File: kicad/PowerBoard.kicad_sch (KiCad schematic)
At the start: 177 parts, among them IC1 LT1910ES8#PBF, IC2 LT1910ES8#PBF, IC3 LT1910ES8#PBF, IC4 LT1910ES8#PBF, IC5 LT1910ES8#PBF, IC7 MAX17541GATB+T, J1 XT90, J10 XT90, J11 XT90, J12 XT90, J13 XT90, J14 DEAN_T, J15 DEAN_T, J16 DEAN_T, J17 DEAN_T, J18 DEAN_T, J19 DEAN_T, J2 DEAN_T, J20 XT60, J21 XT60, J22 XT60, J23 XT60, J24 XT60, J25 XT60, J26 XT60, J27 XT60, J28 XT60, J29 XT60, J3 XT60, J30 XT60, J31 XT60, J32 XT30, J33 XT30, J34 XT30, J35 XT30, J36 XT30, J37 XT30, J38 XT30, J39 XT30, J4 XT30, J40 XT30, J41 XT60, J5 Conn_01x02, J6 XT90, J7 XT90, J8 XT90, J9 XT90, Q1 IRFS7530TRL7PP, Q2 IRFS7437TRLPBF, Q3 IRFS7437TRLPBF, Q4 IRFS7437TRLPBF, Q5 IRFS7437TRLPBF, U1 Pico, U2 INA238, U3 INA238, U4 INA238, U5 INA238, U6 INA238

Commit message: finish v2.4.0
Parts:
- added J42, J43: DEAN_T, SamacSys_Parts:DEANS-T, symbol Connector_Generic:Conn_01x02
- added J44, J45, J46: XT60, Connector_AMASS:AMASS_XT60-F_1x02_P7.20mm_Vertical, symbol Connector_Generic:Conn_01x02
- added J47, J48: XT30, Connector_AMASS:AMASS_XT30U-F_1x02_P5.0mm_Vertical, symbol Connector_Generic:Conn_01x02
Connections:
- net 12V_2: now also J46.2 (Pin_2)
- net 15V_2: now also J44.2 (Pin_2), J45.2 (Pin_2)
- net 24V_2: now also J42.2 (Pin_2), J43.2 (Pin_2)
- net 5V_2: now also J47.2 (Pin_2), J48.2 (Pin_2)
- net GND: now also J42.1 (Pin_1), J43.1 (Pin_1), J44.1 (Pin_1), J45.1 (Pin_1), J46.1 (Pin_1), J47.1 (Pin_1), J48.1 (Pin_1)
- net IC5-SENSE: now reaches C16.2, D24.2 (A), IC5.6 (SENSE), R46.1
- net IC3-SENSE: now reaches C14.1, D22.2 (A), IC3.6 (SENSE), R44.2
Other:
- moved on the sheet: D10, D9

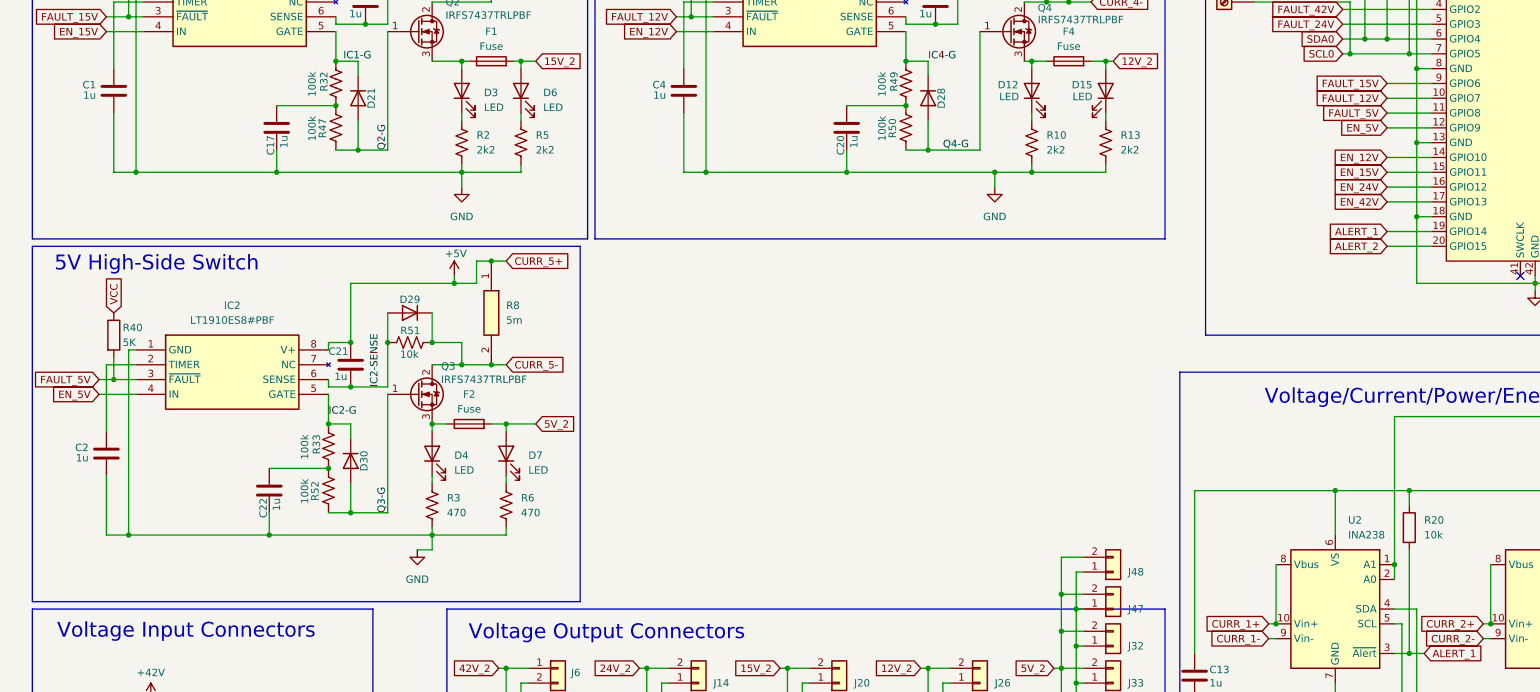
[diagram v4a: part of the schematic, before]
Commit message: rework the 5V switching
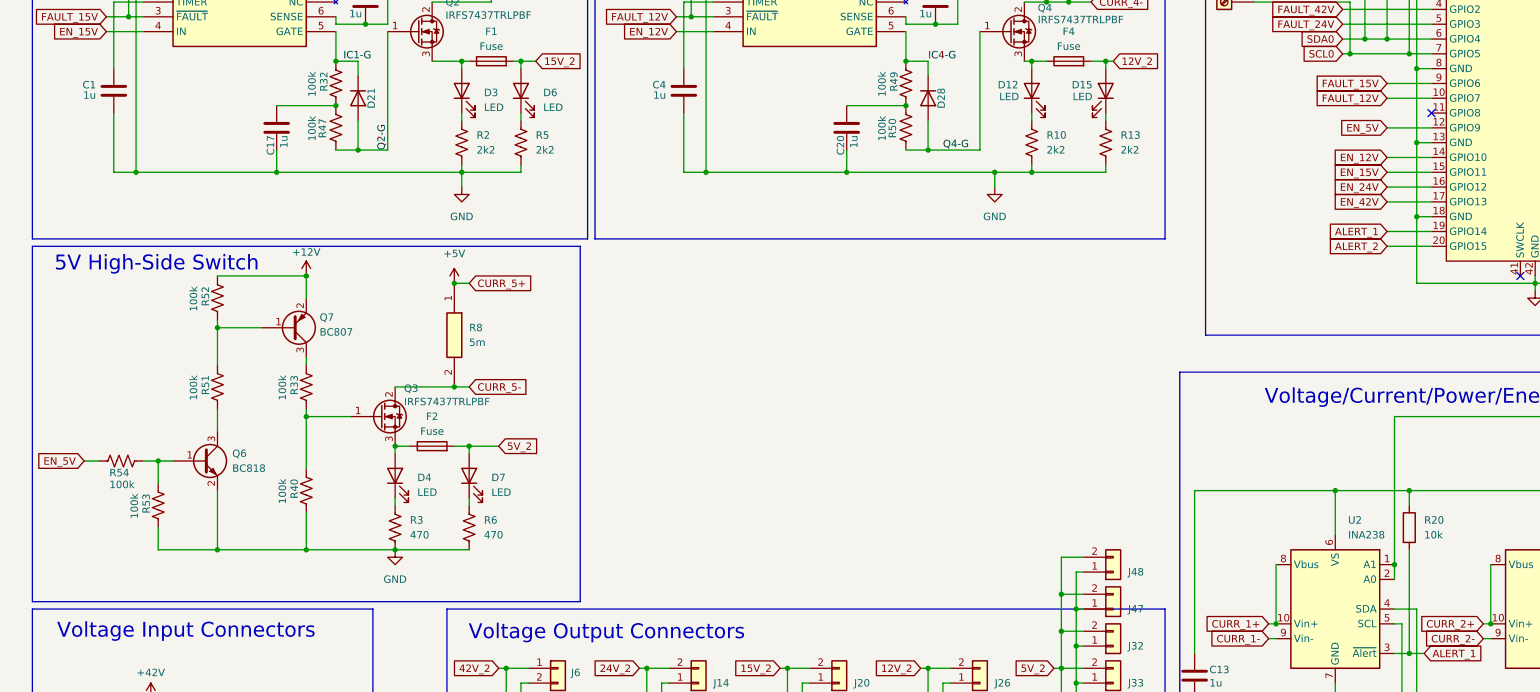
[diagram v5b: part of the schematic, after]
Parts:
- removed C2, C21, C22: 1u, Capacitor_SMD:C_0603_1608Metric, symbol Device:C
- removed D29, D30: 1N4148WT, Diode_SMD:D_SOD-523, symbol Diode:1N4148WT
- removed IC2: LT1910ES8#PBF, SOIC127P599X175-8N, symbol SamacSys_Parts:LT1910ES8#PBF
- removed R40: 5K, Resistor_SMD:R_1206_3216Metric, symbol Device:R
- added Q6: BC818, Package_TO_SOT_SMD:SOT-23, symbol Transistor_BJT:BC818
- added Q7: BC807, Package_TO_SOT_SMD:SOT-23, symbol Transistor_BJT:BC807
- added R40, R53, R54: 100k, Resistor_SMD:R_0603_1608Metric, symbol Device:R_US
- R51: value 10k -> 100k
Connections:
- net +12V: now also R52.2, Q7.2 (E)
- net CURR_5-: no longer R51.2
- net EN_5V: now also R54.2
- net GND: now also Q6.2 (E), R40.1, R53.1
- net at R52.1: now also R51.2, Q7.1 (B); no longer R33.1
- net FAULT_5V: no longer names the net of U1.11 (GPIO8)
- net IC2-G: no longer names the net of R33.2
- net IC2-G: now also Q7.3 (C)
- net IC2-SENSE: no longer names the net of R51.1
- net IC2-SENSE: now also Q6.3 (C)
- net Q3-G: no longer names the net of Q3.1 (G)
- net Q3-G: now also R33.1, R40.2; no longer R52.2
- new net: Q6.1 (B), R53.2, R54.1
- no-connect marks 10 -> 11
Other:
- moved on the sheet: D4, D7, F2, Q3, R3, R6, R8

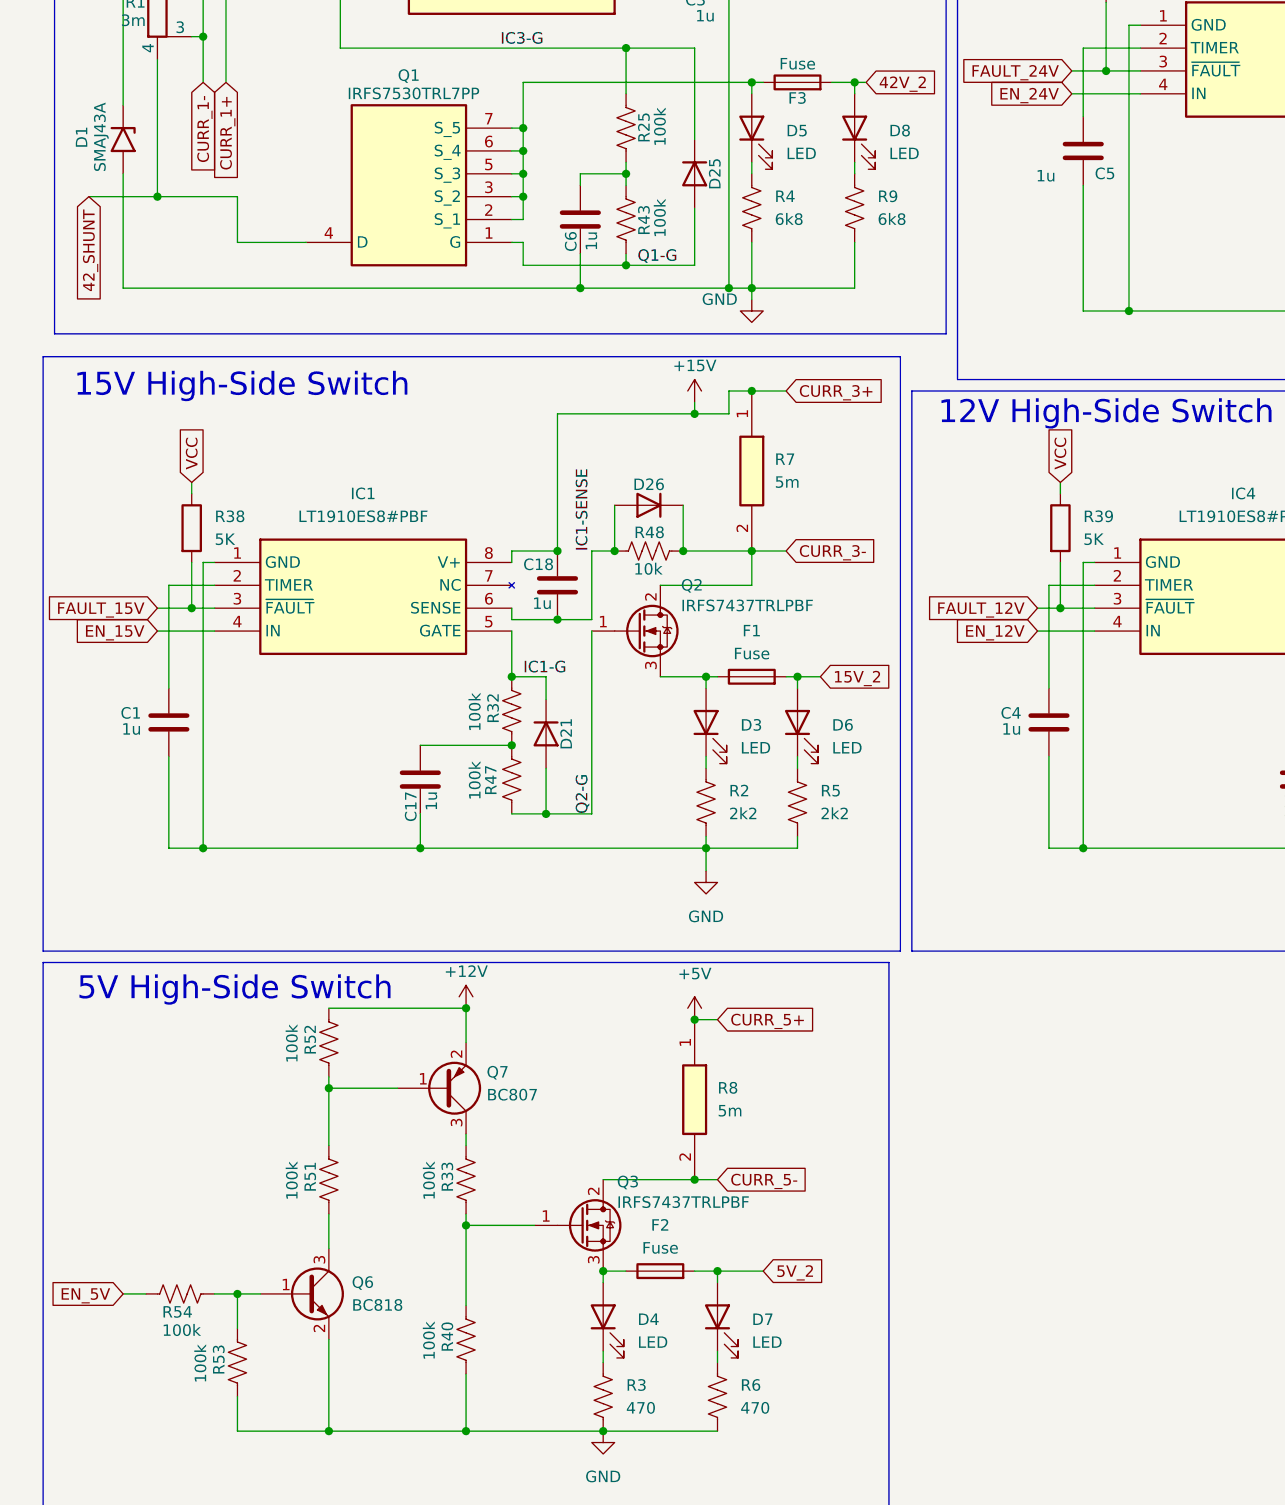
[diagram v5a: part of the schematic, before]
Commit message: adjust component values
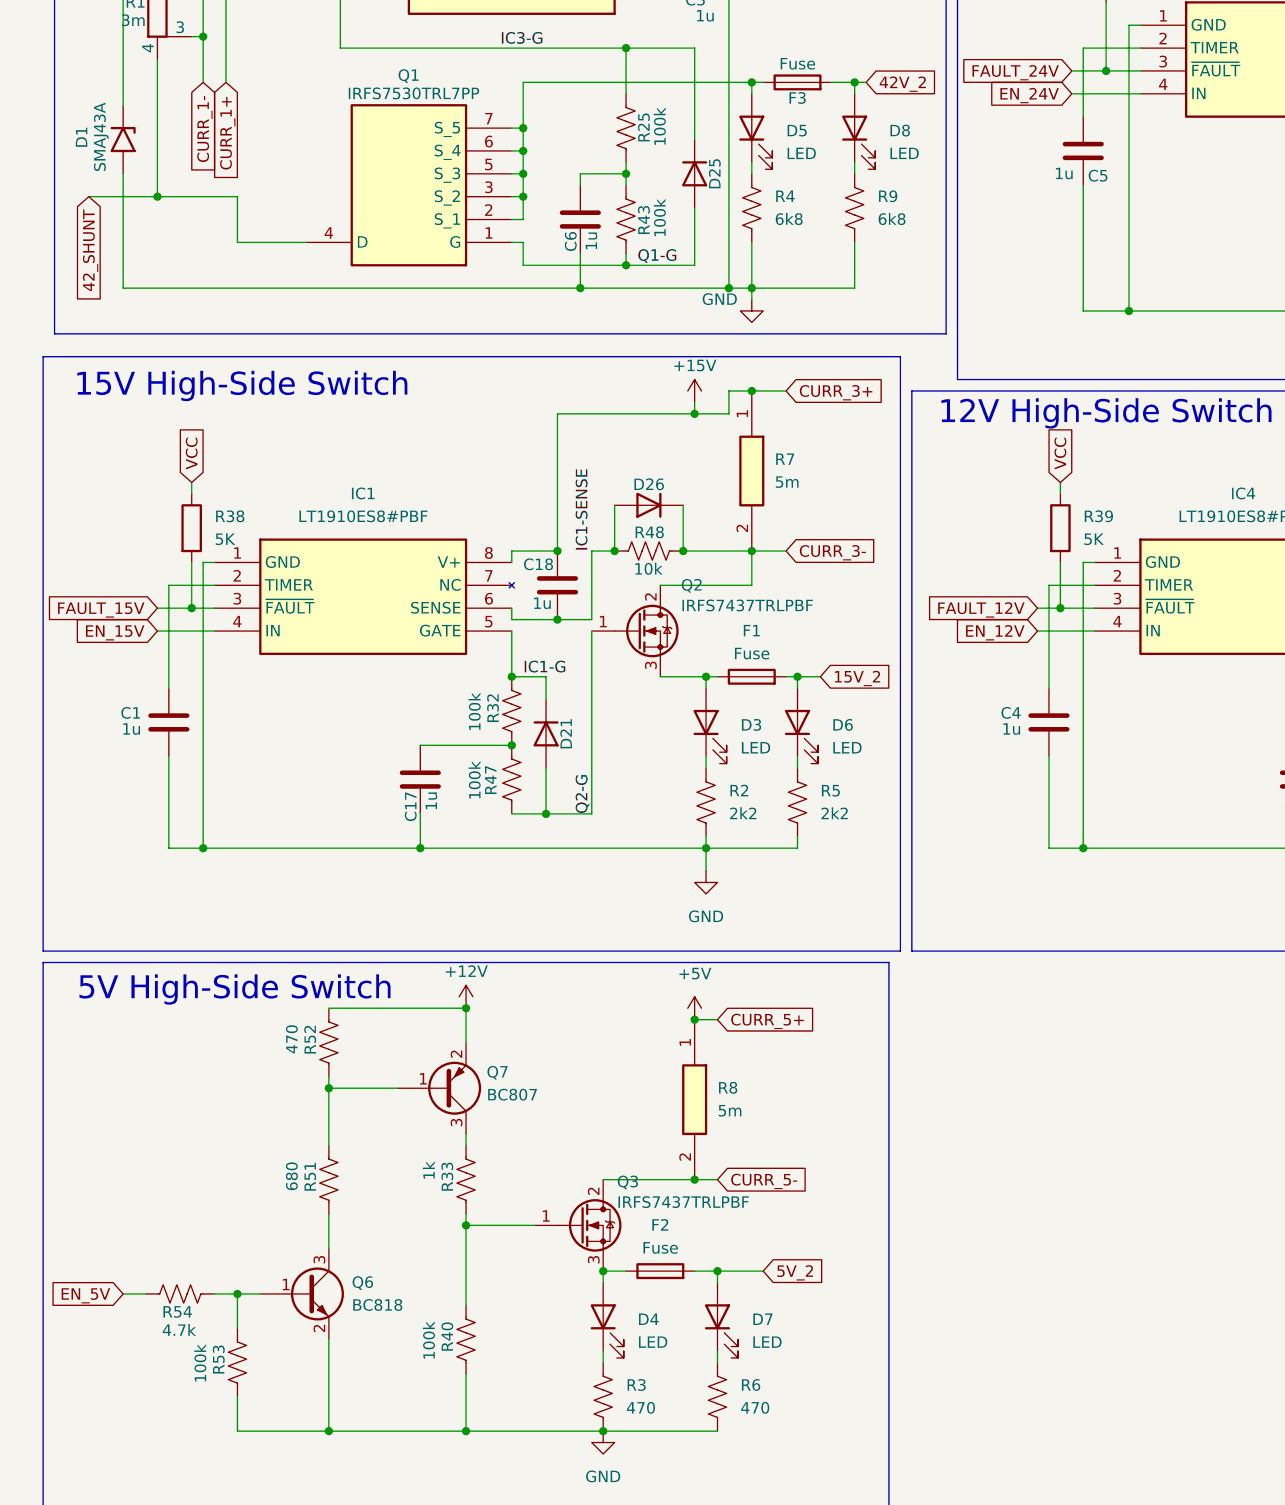
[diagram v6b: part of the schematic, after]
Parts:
- R33: value 100k -> 1k
- R51: value 100k -> 680
- R52: value 100k -> 470
- R54: value 100k -> 4.7k
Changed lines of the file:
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@@
 			)
 		)
-		(property "Value" "100k"
+		(property "Value" "680"
 			(at 40.386 178.308 90)
 			(effects
@@
 			)
 		)
-		(property "Value" "100k"
+		(property "Value" "4.7k"
 			(at 25.908 197.104 90)
 			(effects
@@
 			)
 		)
-		(property "Value" "100k"
+		(property "Value" "1k"
 			(at 55.626 178.308 90)
 			(effects
@@
 		(dnp no)
 		(property "Reference" "C5"
-			(at 129.54 68.58 0)
+			(at 128.778 68.834 0)
 			(effects
 				(font
@@
 		)
 		(property "Value" "1u"
-			(at 125.222 68.834 0)
+			(at 127.254 68.58 0)
 			(effects
 				(font
@@
 			)
 		)
-		(property "Value" "100k"
+		(property "Value" "470"
 			(at 40.386 163.068 90)
 			(effects

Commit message: Generate gerber production files
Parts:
- removed D2: D, Diode_SMD:D_3220_8050Metric, symbol Device:D
- removed D20: D, Diode_SMD:D_1206_3216Metric, symbol Device:D
- removed J5: Conn_01x02, SamacSys_Parts:XT90, symbol Connector_Generic:Conn_01x02
- added D2: BZX84C39, Package_TO_SOT_SMD:SOT-23, symbol Diode:BZX84Cxx
- added Q8: MJD44H11, Package_TO_SOT_SMD:TO-252-2, symbol Transistor_BJT:Q_NPN_BCE
- added R55: 2k7, Resistor_SMD:R_1206_3216Metric, symbol Device:R
- added TP1.1, TP1.2, TP1.3, TP2.1, TP2.2, TP3.1, TP3.2, TP3.3, TP3.4, TP4.1, TP4.2, TP4.3, TP4.4, TP5.1, TP6.1: TestPoint, TestPoint:TestPoint_Pad_1.0x1.0mm, symbol Connector:TestPoint
- C9: value 5.5nF -> 5.6nF
- D1: value SMAJ43A -> SMAJ40A; symbol Diode:SMAJ48A -> Diode:SMAJ40A
- D10: symbol Diode:SMAJ30CA -> Diode:SMAJ15A
- D11: symbol Diode:SMAJ15CA -> Diode:SMAJ12A
- D14: symbol Diode:SMAJ6.5CA -> Diode:SMAJ6.5A
- D9: symbol Diode:SMAJ30CA -> Diode:SMAJ24A
- Q6: value BC818 -> BC817
- R36, R37, R38, R39: value 5K -> 4k7
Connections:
- net +24V: now also TP2.1.1
- net +42V: now also TP1.1.1
- net 42_SHUNT: now also Q8.2 (C), R55.2, TP1.2.1
- net 5V_2: now also D14.2 (A2); no longer D14.1 (A1)
- net CURR_1+: now also TP4.1.1
- net CURR_1-: now also TP4.2.1
- net GND: now also D14.1 (A1), D2.1 (A); no longer D14.2 (A2)
- net IC1-G: now also TP5.1.1
- net IC3-G: now also TP1.3.1
- net IC4-G: now also TP6.1.1
- net IC5-G: now also TP2.2.1
- net SCL1: now also TP4.3.1
- net SDA1: now also TP4.4.1
- net VCC: now also TP3.3.1
- net at C7.1, IC7.2 (VIN), IC7.3 (EN/UVLO): now also Q8.3 (E)
- net at IC7.5 (FB), R16.2, R17.1: now also C8.1, IC7.4 (VCC), TP3.1.1
- net at C9.1, IC7.6 (SS): now also TP3.4.1
- net at IC7.10 (LX), L1.1: now also TP3.2.1
- new net: D2.3 (K), Q8.1 (B), R55.1
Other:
- note added: "Test Points: Battery Voltage High-Side Switch: TP1.1 - kontrola vstupného napätia bateria TP1.2 - napätie pred MOSFETom, kontrola shuntu TP1.3 - kontrola gate drive IC3-Q1 24V High-Side Switch: TP2.1 - kontrola vstupného napätia 24V TP2.2 - výstup drivera LT1910 IC5 AUX: TP3.1 - kontrola VCC/FB TP3.2 - kontrola pred LX TP3.3 - kontrola za LX TP3.4 - kontrola SoftStart INA238: TP4.1 - kontrola U2 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"
- moved on the sheet: C10, C11, C12, C7, C8, C9, IC7, L1, R16, R17, R21
